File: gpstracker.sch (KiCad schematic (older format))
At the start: 53 parts, among them IC1 SIM808, J2 Leds, J3 47553-0001, J4 CONN_COAXIAL, J5 CONN_COAXIAL, J6 Micro_SD_Card, Q1 DMP1045U, SW1 Reset, U1 MCP73832-5-OT, U2 ATMEGA328P-AU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

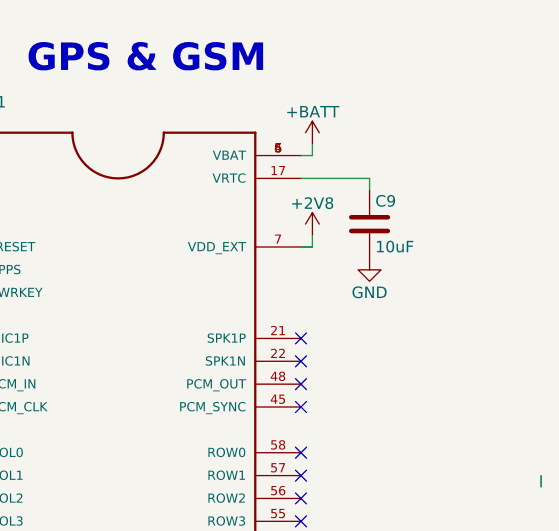
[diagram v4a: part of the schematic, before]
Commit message: Specified conda and resistors. PCB needs to be updated (usb condo from 1210 to 0805)
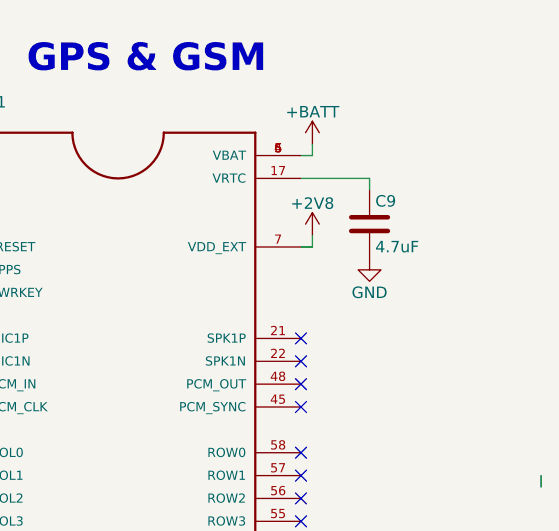
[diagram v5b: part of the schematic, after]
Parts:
- C1, C3: Manufacturer (none) -> Kemet; Manufacturer part number (none) -> C0805X475C4RACTU; Package (none) -> 0805
- C15, C4, C5, C7: Manufacturer (none) -> Kemet; Manufacturer part number (none) -> C0805C104M3RACTU; Package (none) -> 0805
- C2: Manufacturer (none) -> Kemet; Manufacturer part number (none) -> C0805C104M3RACTU
- C6, C8: Manufacturer (none) -> Kemet; Manufacturer part number (none) -> C0805C105K4RACTU; Package (none) -> 0805
- C9: value 10uF -> 4.7uF; Manufacturer (none) -> Kemet; Manufacturer part number (none) -> C0805X475C4RACTU; Package (none) -> 0805
- IC1: Availability Unavailable -> (none); MF Simcom -> (none); MP SIM808 -> (none); Manufacturer (none) -> Simcom; Manufacturer part number (none) -> SIM808; Package None -> (none); Price 18.48 USD -> (none)
- U2: Manufacturer (none) -> Atmel; Manufacturer part number (none) -> ATMEGA328P-AU; Package (none) -> TQFP-32
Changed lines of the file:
@@
 LIBS:freetronics_schematic
 LIBS:custom-power
-LIBS:74xgxx
-LIBS:74xx
-LIBS:ac-dc
-LIBS:actel
-LIBS:adc-dac
-LIBS:allegro
-LIBS:Altera
-LIBS:analog_devices
+LIBS:custom-charge
+LIBS:Amplifier_Audio
+LIBS:Amplifier_Buffer
+LIBS:Amplifier_Current
+LIBS:Amplifier_Difference
+LIBS:Amplifier_Instrumentation
+LIBS:Amplifier_Operational
+LIBS:Amplifier_Video
+LIBS:Analog
+LIBS:Analog_ADC
+LIBS:Analog_DAC
 LIBS:Analog_Switch
-LIBS:analog_switches
-LIBS:atmel
 LIBS:Audio
 LIBS:Battery_Management
-LIBS:bbd
-LIBS:bosch
-LIBS:brooktre
-LIBS:cmos_ieee
-LIBS:cmos4000
-LIBS:conn
+LIBS:Comparator
 LIBS:Connector_Generic
 LIBS:Connector_Generic_Shielded
 LIBS:Connector_Specialized
-LIBS:contrib
 LIBS:Converter_DCDC
 LIBS:CPLD_Altera
-LIBS:cypress
-LIBS:dc-dc
-LIBS:device
-LIBS:digital-audio
+LIBS:CPU
+LIBS:Device
 LIBS:Diode
-LIBS:display
+LIBS:Diode_Laser
 LIBS:Display_Character
 LIBS:Display_Graphic
@@
 LIBS:Driver_FET
 LIBS:Driver_LED
-LIBS:dsp
+LIBS:Driver_Motor
+LIBS:Driver_Relay
 LIBS:DSP_Freescale
 LIBS:DSP_Microchip_DSPIC33
 LIBS:DSP_Texas
-LIBS:elec-unifil
-LIBS:ESD_Protection
 LIBS:FPGA_Actel
-LIBS:ftdi
-LIBS:gennum
 LIBS:Graphic
-LIBS:hc11
-LIBS:intel
-LIBS:interface
+LIBS:Interface
 LIBS:Interface_CAN_LIN
+LIBS:Interface_CurrentLoop
 LIBS:Interface_Ethernet
+LIBS:Interface_Expansion
+LIBS:Interface_HID
+LIBS:Interface_LineDriver
+LIBS:Interface_Optical
 LIBS:Interface_Telecom
+LIBS:Interface_UART
 LIBS:Interface_USB
-LIBS:ir
-LIBS:Lattice
+LIBS:Isolator
+LIBS:Isolator_Analog
+LIBS:Jumper
 LIBS:LED
-LIBS:leds
-LIBS:linear
 LIBS:Logic_74xgxx
 LIBS:Logic_74xx
 LIBS:Logic_CMOS_4000
 LIBS:Logic_CMOS_IEEE
+LIBS:Logic_LevelTranslator
 LIBS:Logic_Programmable
 LIBS:Logic_TTL_IEEE
-LIBS:logo
-LIBS:maxim
 LIBS:MCU_AnalogDevices
+LIBS:MCU_Cypress
 LIBS:MCU_Infineon
 LIBS:MCU_Microchip_PIC10
@@
 LIBS:MCU_Microchip_PIC24
 LIBS:MCU_Microchip_PIC32
+LIBS:MCU_Microchip_SAME
+LIBS:MCU_Microchip_SAML
+LIBS:MCU_NXP_HC11
 LIBS:MCU_NXP_Kinetis
 LIBS:MCU_NXP_LPC
@@
 LIBS:MCU_ST_STM8
 LIBS:MCU_ST_STM32
+LIBS:MCU_Texas
 LIBS:MCU_Texas_MSP430
 LIBS:Mechanical
-LIBS:memory
+LIBS:Memory_Controller
 LIBS:Memory_EEPROM
 LIBS:Memory_Flash
 LIBS:Memory_NVRAM
 LIBS:Memory_RAM
-LIBS:microchip
-LIBS:microchip_dspic33dsc
-LIBS:microchip_pic10mcu
-LIBS:microchip_pic12mcu
-LIBS:microchip_pic16mcu
-LIBS:microchip_pic18mcu
-LIBS:microchip_pic24mcu
-LIBS:microchip_pic32mcu
-LIBS:microcontrollers
-LIBS:modules
+LIBS:Memory_UniqueID
 LIBS:Motor
-LIBS:motor_drivers
-LIBS:motorola
-LIBS:motors
-LIBS:msp430
-LIBS:nordicsemi
-LIBS:nxp
-LIBS:nxp_armmcu
-LIBS:onsemi
-LIBS:opto
 LIBS:Oscillator
-LIBS:Oscillators
-LIBS:philips
 LIBS:Potentiometer_Digital
 LIBS:power
 LIBS:Power_Management
 LIBS:Power_Protection
-LIBS:powerint
+LIBS:Power_Supervisor
 LIBS:pspice
 LIBS:Reference_Current
 LIBS:Reference_Voltage
-LIBS:references
-LIBS:regul
 LIBS:Regulator_Controller
 LIBS:Regulator_Current
@@
 LIBS:Regulator_Switching
 LIBS:Relay
-LIBS:relays
+LIBS:Relay_SolidState
 LIBS:RF_AM_FM
 LIBS:RF_Bluetooth
+LIBS:RF_Mixer
 LIBS:RF_Module
+LIBS:RF_RFID
 LIBS:RF_WiFi
-LIBS:rfcom
 LIBS:Sensor
 LIBS:Sensor_Audio
@@
 LIBS:Sensor_Optical
 LIBS:Sensor_Pressure
+LIBS:Sensor_Proximity
 LIBS:Sensor_Temperature
 LIBS:Sensor_Touch
 LIBS:Sensor_Voltage
-LIBS:sensors
-LIBS:silabs
-LIBS:siliconi
-LIBS:stm8
-LIBS:stm32
-LIBS:supertex
 LIBS:Switch
-LIBS:switches
-LIBS:texas
 LIBS:Timer
-LIBS:transf
+LIBS:Timer_RTC
 LIBS:Transformer
+LIBS:Transistor_Array
 LIBS:Transistor_BJT
 LIBS:Transistor_FET
 LIBS:Transistor_IGBT
-LIBS:transistors
-LIBS:triac_thyristor
-LIBS:ttl_ieee
 LIBS:Valve
-LIBS:valves
-LIBS:video
-LIBS:wiznet
-LIBS:Worldsemi
-LIBS:Xicor
-LIBS:xilinx
-LIBS:zetex
-LIBS:Zilog
-LIBS:custom-charge
+LIBS:Video
 LIBS:gpstracker-cache
 EELAYER 25 0
@@
 F 2 "Housings_QFP:TQFP-32_7x7mm_Pitch0.8mm" H 2050 4300 50  0001 C CIN
 F 3 "" H 2050 4300 50  0001 C CNN
+F 4 "Atmel" H 2050 4300 60  0001 C CNN "Manufacturer"
+F 5 "ATMEGA328P-AU" H 2050 4300 60  0001 C CNN "Manufacturer part number"
+F 6 "TQFP-32" H 2050 4300 60  0001 C CNN "Package"
 	1    2050 4300
 	1    0    0    -1
@@
 F 2 "Capacitors_SMD:C_0805_HandSoldering" H 688 950 50  0001 C CNN
 F 3 "" H 650 1100 50  0001 C CNN
+F 4 "Kemet" H 650 1100 60  0001 C CNN "Manufacturer"
+F 5 "C0805X475C4RACTU" H 650 1100 60  0001 C CNN "Manufacturer part number"
+F 6 "0805" H 650 1100 60  0001 C CNN "Package"
 	1    650  1100
 	-1   0    0    1
@@
 F 2 "Capacitors_SMD:C_0805_HandSoldering" H 2438 1550 50  0001 C CNN
 F 3 "" H 2400 1700 50  0001 C CNN
+F 4 "Kemet" H 2400 1700 60  0001 C CNN "Manufacturer"
+F 5 "C0805X475C4RACTU" H 2400 1700 60  0001 C CNN "Manufacturer part number"
+F 6 "0805" H 2400 1700 60  0001 C CNN "Package"
 	1    2400 1700
 	1    0    0    -1
@@
 F 2 "Capacitors_SMD:C_0805_HandSoldering" H 4388 4750 50  0001 C CNN
 F 3 "" H 4350 4900 50  0001 C CNN
+F 4 "Kemet" H 4350 4900 60  0001 C CNN "Manufacturer"
+F 5 "C0805C104M3RACTU" H 4350 4900 60  0001 C CNN "Manufacturer part number"
+F 6 "0805" H 4350 4900 60  0001 C CNN "Package"
 	1    4350 4900
 	1    0    0    -1
@@
 F 2 "Capacitors_SMD:C_0805_HandSoldering" H 1038 3850 50  0001 C CNN
 F 3 "" H 1000 4000 50  0001 C CNN
+F 4 "Kemet" H 1000 4000 60  0001 C CNN "Manufacturer"
+F 5 "C0805C104M3RACTU" H 1000 4000 60  0001 C CNN "Manufacturer part number"
 	1    1000 4000
 	1    0    0    -1
@@
 F 2 "Capacitors_SMD:C_0805_HandSoldering" H 5538 1050 50  0001 C CNN
 F 3 "" H 5500 1200 50  0001 C CNN
+F 4 "Kemet" H 5500 1200 60  0001 C CNN "Manufacturer"
+F 5 "C0805C105K4RACTU" H 5500 1200 60  0001 C CNN "Manufacturer part number"
+F 6 "0805" H 5500 1200 60  0001 C CNN "Package"
 	1    5500 1200
 	1    0    0    -1
@@
 F 2 "Capacitors_SMD:C_0805_HandSoldering" H 4688 1050 50  0001 C CNN
 F 3 "" H 4650 1200 50  0001 C CNN
+F 4 "Kemet" H 4650 1200 60  0001 C CNN "Manufacturer"
+F 5 "C0805C105K4RACTU" H 4650 1200 60  0001 C CNN "Manufacturer part number"
+F 6 "0805" H 4650 1200 60  0001 C CNN "Package"
 	1    4650 1200
 	1    0    0    -1
@@
 F 2 "Capacitors_SMD:C_0805_HandSoldering" H 3888 6650 50  0001 C CNN
 F 3 "" H 3850 6800 50  0001 C CNN
+F 4 "Kemet" H 3850 6800 60  0001 C CNN "Manufacturer"
+F 5 "C0805C104M3RACTU" H 3850 6800 60  0001 C CNN "Manufacturer part number"
+F 6 "0805" H 3850 6800 60  0001 C CNN "Package"
 	1    3850 6800
 	0    1    1    0
@@
 F 2 "Capacitors_SMD:C_0805_HandSoldering" H 4888 6450 50  0001 C CNN
 F 3 "" H 4850 6600 50  0001 C CNN
+F 4 "Kemet" H 4850 6600 60  0001 C CNN "Manufacturer"
+F 5 "C0805C104M3RACTU" H 4850 6600 60  0001 C CNN "Manufacturer part number"
+F 6 "0805" H 4850 6600 60  0001 C CNN "Package"
 	1    4850 6600
 	1    0    0    -1
@@
 F 2 "SIM808:QFN100P2400X2400X260-68N" H 9600 3350 50  0001 L BNN
 F 3 "Module: GPS/GSM; GPRS; 2G; 1800MHz, 900MHz; GPIO, Serial, USB; SMD" H 9600 3350 50  0001 L BNN
-F 4 "Simcom" H 9600 3350 50  0001 L BNN "MF"
-F 5 "Unavailable" H 9600 3350 50  0001 L BNN "Availability"
-F 6 "18.48 USD" H 9600 3350 50  0001 L BNN "Price"
-F 7 "SIM808" H 9600 3350 50  0001 L BNN "MP"
-F 8 "None" H 9600 3350 50  0001 L BNN "Package"
+F 4 "Simcom" H 9600 3350 50  0001 L BNN "Manufacturer"
+F 5 "SIM808" H 9600 3350 50  0001 L BNN "Manufacturer part number"
 	1    9600 3350
 	1    0    0    -1
@@
 P 10700 1450
 F 0 "C9" H 10725 1550 50  0000 L CNN
-F 1 "10uF" H 10725 1350 50  0000 L CNN
+F 1 "4.7uF" H 10725 1350 50  0000 L CNN
 F 2 "Capacitors_SMD:C_0805_HandSoldering" H 10738 1300 50  0001 C CNN
 F 3 "" H 10700 1450 50  0001 C CNN
+F 4 "Kemet" H 10700 1450 60  0001 C CNN "Manufacturer"
+F 5 "C0805X475C4RACTU" H 10700 1450 60  0001 C CNN "Manufacturer part number"
+F 6 "0805" H 10700 1450 60  0001 C CNN "Package"
 	1    10700 1450
 	1    0    0    -1
@@
 F 2 "Capacitors_SMD:C_0805_HandSoldering" H 838 3350 50  0001 C CNN
 F 3 "" H 800 3500 50  0001 C CNN
+F 4 "Kemet" H 800 3500 60  0001 C CNN "Manufacturer"
+F 5 "C0805C104M3RACTU" H 800 3500 60  0001 C CNN "Manufacturer part number"
+F 6 "0805" H 800 3500 60  0001 C CNN "Package"
 	1    800  3500
 	1    0    0    -1

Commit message: Made the usb connector vertical
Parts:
- ICSP1: footprint Pin_Headers:Pin_Header_Straight_2x03_Pitch2.54mm -> custom-conn:VASCH3x2
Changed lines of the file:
@@
 F 0 "ICSP1" H 2350 7300 50  0000 C CNN
 F 1 "CONN_02X03" H 2350 6900 50  0000 C CNN
-F 2 "Pin_Headers:Pin_Header_Straight_2x03_Pitch2.54mm" H 2350 5900 50  0001 C CNN
+F 2 "custom-conn:VASCH3x2" H 2350 5900 50  0001 C CNN
 F 3 "" H 2350 5900 50  0001 C CNN
 	1    2350 7100

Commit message: Ordered PCB
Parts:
- BT1: Manufacturer (none) -> JST; Manufacturer part number (none) -> S2B-PH-SM4-TB
- BT2: Manufacturer (none) -> Keystone; Manufacturer part number (none) -> 1058
- C17: Manufacturer (none) -> Kemet; Manufacturer part number (none) -> C0805C330K4HACAUTO; Package (none) -> 0805
- C18: Manufacturer (none) -> Kemet; Manufacturer part number (none) -> C0805C100K4HACAUTO; Package (none) -> 0805
- D1: Manufacturer (none) -> ON Semiconductor; Manufacturer part number (none) -> MMSZ5231BT1G; Package (none) -> SOD-123-2
- D3: Manufacturer (none) -> Diodes Incorporated; Manufacturer part number (none) -> B130LAW-7-F; Package (none) -> SOD123
- ICSP1: Manufacturer (none) -> FCI; Manufacturer part number (none) -> 75869-131LF
- J3: Manufacturer (none) -> Molex; Manufacturer part number (none) -> 47553-0001
- J4, J5: Manufacturer (none) -> Linx Technologies; Manufacturer part number (none) -> CONUFL001-SMD
- J6: Manufacturer (none) -> Molex; Manufacturer part number (none) -> 104031-0811
- LED1, LED4: Manufacturer (none) -> Kingbright; Manufacturer part number (none) -> APT2012SECK; Package (none) -> 0805
- LED2, LED3: Manufacturer (none) -> Kingbright; Manufacturer part number (none) -> APT2012SGC; Package (none) -> 0805
- LED5: Manufacturer (none) -> Kingbright; Manufacturer part number (none) -> APT2012EC
- Q1: Manufacturer (none) -> Diodes Incorporated; Manufacturer part number (none) -> DMP1045U-7; Package (none) -> SOT-23-3
- R1: Manufacturer (none) -> Panasonic; Manufacturer part number (none) -> ERJ-6GEYJ202V; Package (none) -> 0805
- R10, R2, R4, R5, R8, R9: Manufacturer (none) -> Panasonic; Manufacturer part number (none) -> ERJ-6GEYJ102V; Package (none) -> 0805
- R11: Manufacturer (none) -> Panasonic; Manufacturer part number (none) -> ERJ-6GEYJ161V; Package (none) -> 0805
- R12: Manufacturer (none) -> Panasonic; Manufacturer part number (none) -> ERJ-6GEYJ203V; Package (none) -> 0805
- R13, R6: Manufacturer (none) -> Panasonic; Manufacturer part number (none) -> ERJ-6GEYJ103V; Package (none) -> 0805
- R14, R15: value 50k -> 51k; Manufacturer (none) -> Panasonic; Manufacturer part number (none) -> ERJ-6GEYJ513V; Package (none) -> 0805
- R3: value 470R -> 1k; Manufacturer (none) -> Panasonic; Manufacturer part number (none) -> ERJ-6GEYJ102V; Package (none) -> 0805
- R7: Manufacturer (none) -> Panasonic; Manufacturer part number (none) -> ERJ-6GEYJ104V; Package (none) -> 0805
- SW1: footprint Buttons_Switches_SMD:SW_SPST_EVPBF -> Buttons_Switches_SMD:SW_SPST_B3S-1000; Manufacturer (none) -> Omron; Manufacturer part number (none) -> B3S-1000
- TV1: Manufacturer (none) -> ON Semiconductor; Manufacturer part number (none) -> SMF05C; Package (none) -> SOT-363
- U1: Manufacturer (none) -> Microchip; Manufacturer part number (none) -> MCP73832T-5ACI/OT; Package (none) -> SOT-23
- U3: Manufacturer (none) -> Microchip; Manufacturer part number (none) -> 24LC512T-I/SN; Package (none) -> SOIC-8
- U4: Manufacturer (none) -> Microchip; Manufacturer part number (none) -> MCP1700T-3302E/TT; Package (none) -> SOT-23-3
- U5: Manufacturer (none) -> Maxim Integrated; Manufacturer part number (none) -> DS3231SN#; Package (none) -> SOIC-16

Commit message: Fixed references for 4.7uF capacitor
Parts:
- C1, C3, C9: Manufacturer part number C0805X475C4RACTU -> C0805X475J4RACAUTO
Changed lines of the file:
@@
 F 3 "" H 650 1100 50  0001 C CNN
 F 4 "Kemet" H 650 1100 60  0001 C CNN "Manufacturer"
-F 5 "C0805X475C4RACTU" H 650 1100 60  0001 C CNN "Manufacturer part number"
+F 5 "C0805X475J4RACAUTO" H 650 1100 60  0001 C CNN "Manufacturer part number"
 F 6 "0805" H 650 1100 60  0001 C CNN "Package"
 	1    650  1100
@@
 F 3 "" H 2400 1700 50  0001 C CNN
 F 4 "Kemet" H 2400 1700 60  0001 C CNN "Manufacturer"
-F 5 "C0805X475C4RACTU" H 2400 1700 60  0001 C CNN "Manufacturer part number"
+F 5 "C0805X475J4RACAUTO" H 2400 1700 60  0001 C CNN "Manufacturer part number"
 F 6 "0805" H 2400 1700 60  0001 C CNN "Package"
 	1    2400 1700
@@
 F 3 "" H 10700 1450 50  0001 C CNN
 F 4 "Kemet" H 10700 1450 60  0001 C CNN "Manufacturer"
-F 5 "C0805X475C4RACTU" H 10700 1450 60  0001 C CNN "Manufacturer part number"
+F 5 "C0805X475J4RACAUTO" H 10700 1450 60  0001 C CNN "Manufacturer part number"
 F 6 "0805" H 10700 1450 60  0001 C CNN "Package"
 	1    10700 1450
